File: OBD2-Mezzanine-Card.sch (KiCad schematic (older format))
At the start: 18 parts, among them P1 CONN_02X20

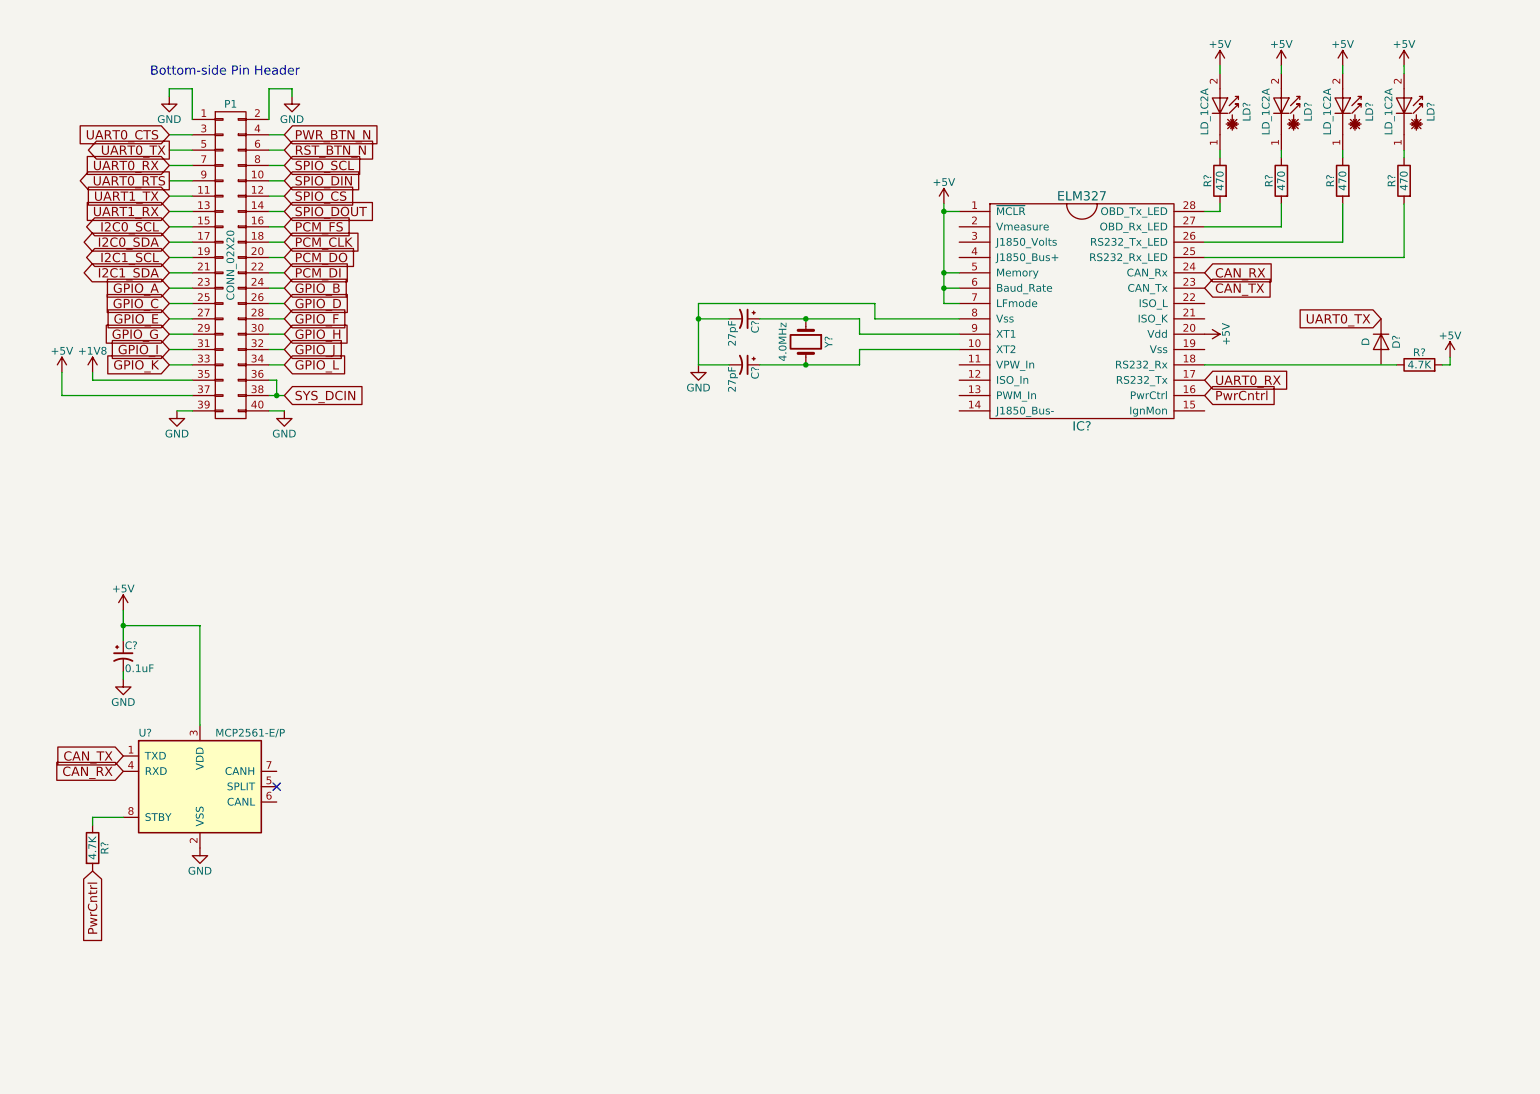
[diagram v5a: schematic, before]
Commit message: sch: Add some more connections
Signed-off-by: Alistair Francis <alistair@alistair23.me>
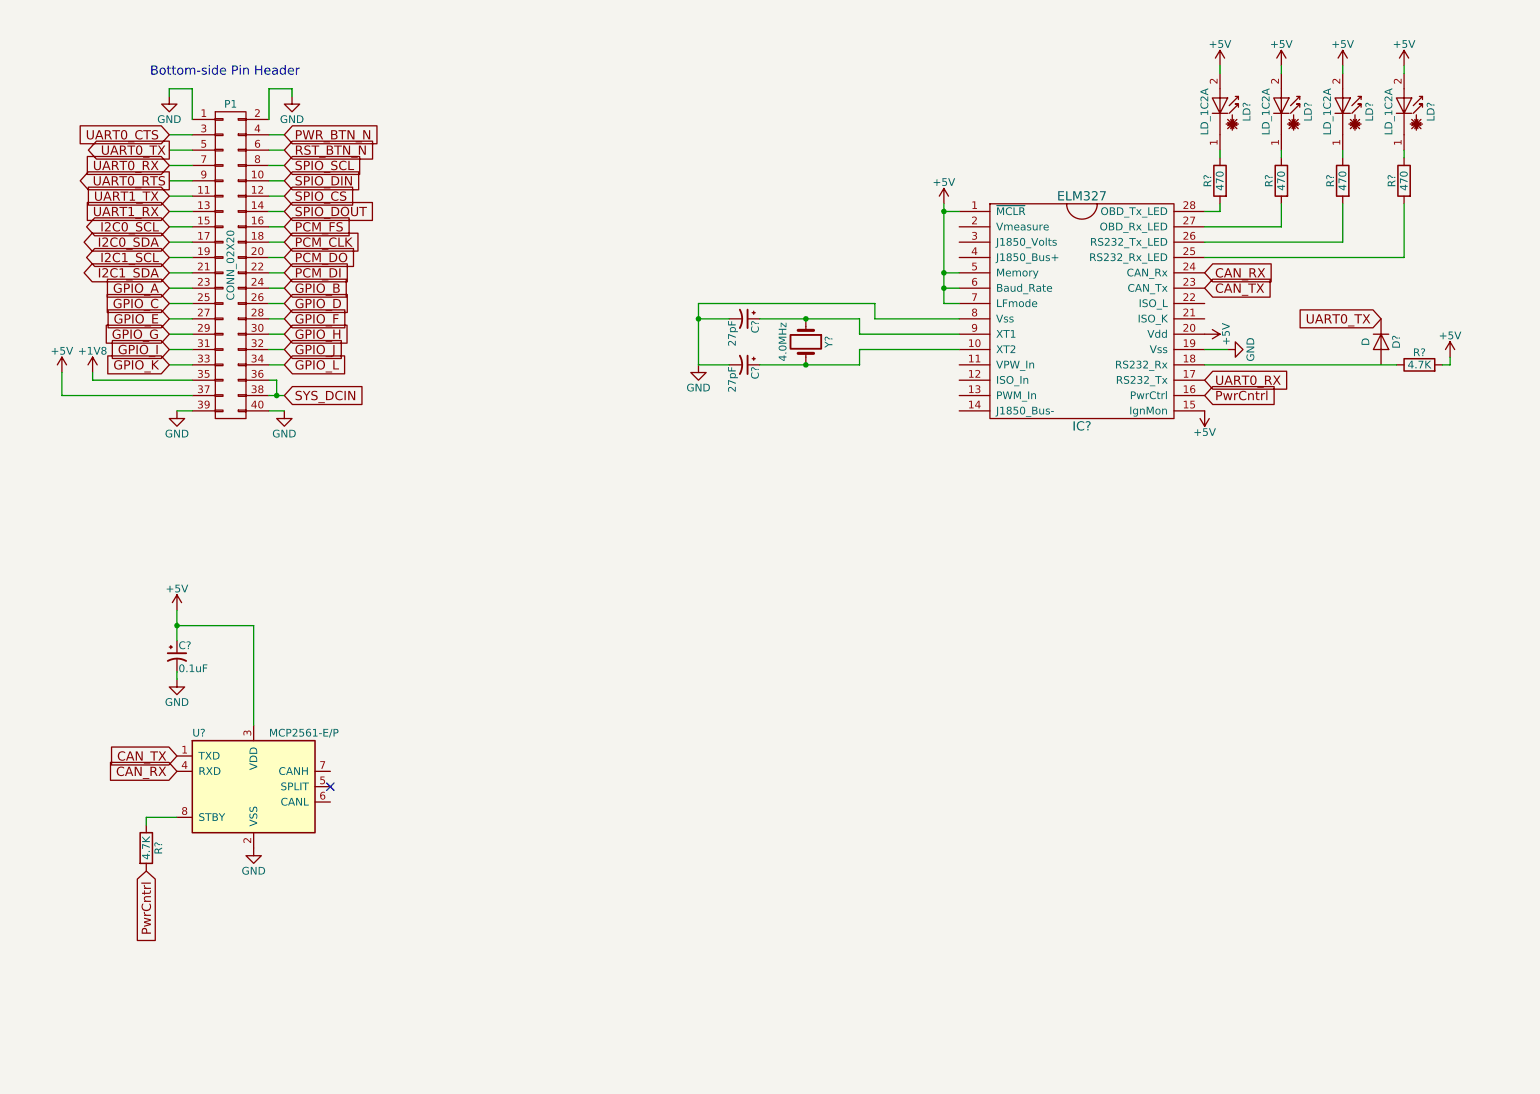
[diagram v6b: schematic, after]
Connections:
- net +5V: now also IC?.15 (IgnMon)
- net GND: now also IC?.19 (Vss)
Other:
- moved on the sheet: C?, R?, U?
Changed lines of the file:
@@
 L MCP2561-E/P U?
 U 1 1 5AA61DC4
-P 1900 5700
-F 0 "U?" H 1500 6050 50  0000 L CNN
-F 1 "MCP2561-E/P" H 2000 6050 50  0000 L CNN
-F 2 "Housings_DIP:DIP-8_W7.62mm" H 1900 5200 50  0001 C CIN
-F 3 "" H 1900 5700 50  0001 C CNN
-	1    1900 5700
+P 2250 5700
+F 0 "U?" H 1850 6050 50  0000 L CNN
+F 1 "MCP2561-E/P" H 2350 6050 50  0000 L CNN
+F 2 "Housings_DIP:DIP-8_W7.62mm" H 2250 5200 50  0001 C CIN
+F 3 "" H 2250 5700 50  0001 C CNN
+	1    2250 5700
 	1    0    0    -1
 $EndComp
-Text GLabel 1400 5600 0    60   Input ~ 0
+Text GLabel 1750 5600 0    60   Input ~ 0
 CAN_RX
 Text GLabel 8450 2350 2    60   Input ~ 0
@@
 Text GLabel 8450 2450 2    60   Input ~ 0
 CAN_TX
-Text GLabel 1400 5500 0    60   Input ~ 0
+Text GLabel 1750 5500 0    60   Input ~ 0
 CAN_TX
 $Comp
 L GND #PWR?
 U 1 1 5AA5FF31
-P 1900 6100
-F 0 "#PWR?" H 1900 5850 50  0001 C CNN
-F 1 "GND" H 1900 5950 50  0000 C CNN
-F 2 "" H 1900 6100 50  0001 C CNN
-F 3 "" H 1900 6100 50  0001 C CNN
-	1    1900 6100
+P 2250 6100
+F 0 "#PWR?" H 2250 5850 50  0001 C CNN
+F 1 "GND" H 2250 5950 50  0000 C CNN
+F 2 "" H 2250 6100 50  0001 C CNN
+F 3 "" H 2250 6100 50  0001 C CNN
+	1    2250 6100
 	1    0    0    -1
 $EndComp
@@
 L +5V #PWR?
 U 1 1 5AA5FFA4
-P 1400 4550
-F 0 "#PWR?" H 1400 4400 50  0001 C CNN
-F 1 "+5V" H 1400 4690 50  0000 C CNN
-F 2 "" H 1400 4550 50  0001 C CNN
-F 3 "" H 1400 4550 50  0001 C CNN
-	1    1400 4550
+P 1750 4550
+F 0 "#PWR?" H 1750 4400 50  0001 C CNN
+F 1 "+5V" H 1750 4690 50  0000 C CNN
+F 2 "" H 1750 4550 50  0001 C CNN
+F 3 "" H 1750 4550 50  0001 C CNN
+	1    1750 4550
 	1    0    0    -1
 $EndComp
@@
 L CP1_Small C?
 U 1 1 5AA5FFD8
-P 1400 4850
-F 0 "C?" H 1410 4920 50  0000 L CNN
-F 1 "0.1uF" H 1410 4770 50  0000 L CNN
-F 2 "" H 1400 4850 50  0001 C CNN
-F 3 "" H 1400 4850 50  0001 C CNN
-	1    1400 4850
+P 1750 4850
+F 0 "C?" H 1760 4920 50  0000 L CNN
+F 1 "0.1uF" H 1760 4770 50  0000 L CNN
+F 2 "" H 1750 4850 50  0001 C CNN
+F 3 "" H 1750 4850 50  0001 C CNN
+	1    1750 4850
 	1    0    0    -1
 $EndComp
@@
 L GND #PWR?
 U 1 1 5AA600BE
-P 1400 5000
-F 0 "#PWR?" H 1400 4750 50  0001 C CNN
-F 1 "GND" H 1400 4850 50  0000 C CNN
-F 2 "" H 1400 5000 50  0001 C CNN
-F 3 "" H 1400 5000 50  0001 C CNN
-	1    1400 5000
+P 1750 5000
+F 0 "#PWR?" H 1750 4750 50  0001 C CNN
+F 1 "GND" H 1750 4850 50  0000 C CNN
+F 2 "" H 1750 5000 50  0001 C CNN
+F 3 "" H 1750 5000 50  0001 C CNN
+	1    1750 5000
 	1    0    0    -1
 $EndComp
 Wire Wire Line
-	1400 4550 1400 4750
+	1750 4550 1750 4750
 Wire Wire Line
-	1400 4950 1400 5000
+	1750 4950 1750 5000
 Wire Wire Line
-	1400 4650 1900 4650
+	1750 4650 2250 4650
 Wire Wire Line
-	1900 4650 1900 5300
-Connection ~ 1400 4650
+	2250 4650 2250 5300
+Connection ~ 1750 4650
 $Comp
 L R R?
 U 1 1 5AA6032D
-P 1200 6100
-F 0 "R?" V 1280 6100 50  0000 C CNN
-F 1 "4.7K" V 1200 6100 50  0000 C CNN
-F 2 "" V 1130 6100 50  0001 C CNN
-F 3 "" H 1200 6100 50  0001 C CNN
-	1    1200 6100
+P 1550 6100
+F 0 "R?" V 1630 6100 50  0000 C CNN
+F 1 "4.7K" V 1550 6100 50  0000 C CNN
+F 2 "" V 1480 6100 50  0001 C CNN
+F 3 "" H 1550 6100 50  0001 C CNN
+	1    1550 6100
 	1    0    0    -1
 $EndComp
 Text GLabel 8450 3150 2    60   Input ~ 0
 PwrCntrl
-Text GLabel 1200 6250 3    60   Input ~ 0
+Text GLabel 1550 6250 3    60   Input ~ 0
 PwrCntrl
 Wire Wire Line
-	1400 5900 1200 5900
+	1750 5900 1550 5900
 Wire Wire Line
-	1200 5900 1200 5950
-NoConn ~ 2400 5700
+	1550 5900 1550 5950
+NoConn ~ 2750 5700
+$Comp
+L +5V #PWR?
+U 1 1 5AA61411
+P 8450 3250
+F 0 "#PWR?" H 8450 3100 50  0001 C CNN
+F 1 "+5V" H 8450 3390 50  0000 C CNN
+F 2 "" H 8450 3250 50  0001 C CNN
+F 3 "" H 8450 3250 50  0001 C CNN
+	1    8450 3250
+	-1   0    0    1
+$EndComp
+$Comp
+L GND #PWR?
+U 1 1 5AA61537
+P 8600 2850
+F 0 "#PWR?" H 8600 2600 50  0001 C CNN
+F 1 "GND" H 8600 2700 50  0000 C CNN
+F 2 "" H 8600 2850 50  0001 C CNN
+F 3 "" H 8600 2850 50  0001 C CNN
+	1    8600 2850
+	0    -1   -1   0
+$EndComp
+Wire Wire Line
+	8600 2850 8450 2850
 $EndSCHEMATC

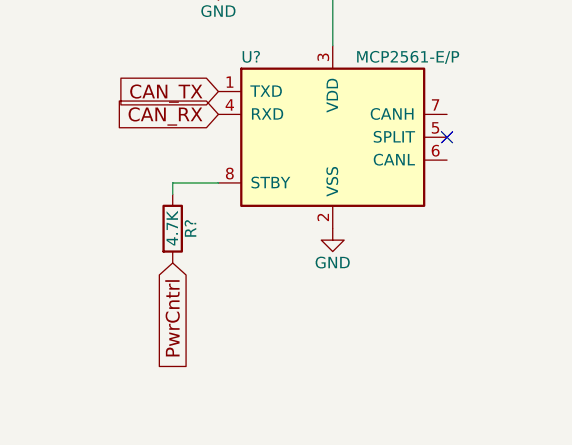
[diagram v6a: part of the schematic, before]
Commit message: sch: Fixup a mistake
Signed-off-by: Alistair Francis <alistair@alistair23.me>
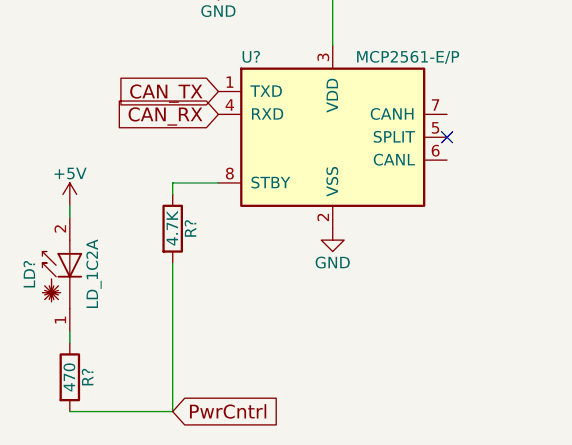
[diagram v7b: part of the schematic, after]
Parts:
- added LD?: LD_1C2A, symbol Laserdiode_1C2A
- added R?: 470, symbol R
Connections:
- net +5V: now also LD?.2 (A)
- net PwrCntrl: now also R?.2
- new net: LD?.1 (K), R?.1
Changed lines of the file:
@@
 Text GLabel 8450 3150 2    60   Input ~ 0
 PwrCntrl
-Text GLabel 1550 6250 3    60   Input ~ 0
+Text GLabel 1550 6900 2    60   Input ~ 0
 PwrCntrl
 Wire Wire Line
@@
 Wire Wire Line
 	8600 2850 8450 2850
+$Comp
+L +5V #PWR?
+U 1 1 5AA61B64
+P 1100 6000
+F 0 "#PWR?" H 1100 5850 50  0001 C CNN
+F 1 "+5V" H 1100 6140 50  0000 C CNN
+F 2 "" H 1100 6000 50  0001 C CNN
+F 3 "" H 1100 6000 50  0001 C CNN
+	1    1100 6000
+	1    0    0    -1
+$EndComp
+$Comp
+L Laserdiode_1C2A LD?
+U 1 1 5AA61B9C
+P 1100 6250
+F 0 "LD?" H 1050 6425 50  0000 C CNN
+F 1 "LD_1C2A" H 1050 6150 50  0000 C CNN
+F 2 "" H 1000 6225 50  0001 C CNN
+F 3 "" H 1130 6050 50  0001 C CNN
+	1    1100 6250
+	0    -1   -1   0
+$EndComp
+$Comp
+L R R?
+U 1 1 5AA63138
+P 1100 6750
+F 0 "R?" V 1180 6750 50  0000 C CNN
+F 1 "470" V 1100 6750 50  0000 C CNN
+F 2 "" V 1030 6750 50  0001 C CNN
+F 3 "" H 1100 6750 50  0001 C CNN
+	1    1100 6750
+	1    0    0    -1
+$EndComp
+Wire Wire Line
+	1100 6000 1100 6050
+Wire Wire Line
+	1100 6550 1100 6600
+Wire Wire Line
+	1100 6900 1550 6900
+Wire Wire Line
+	1550 6900 1550 6250
 $EndSCHEMATC

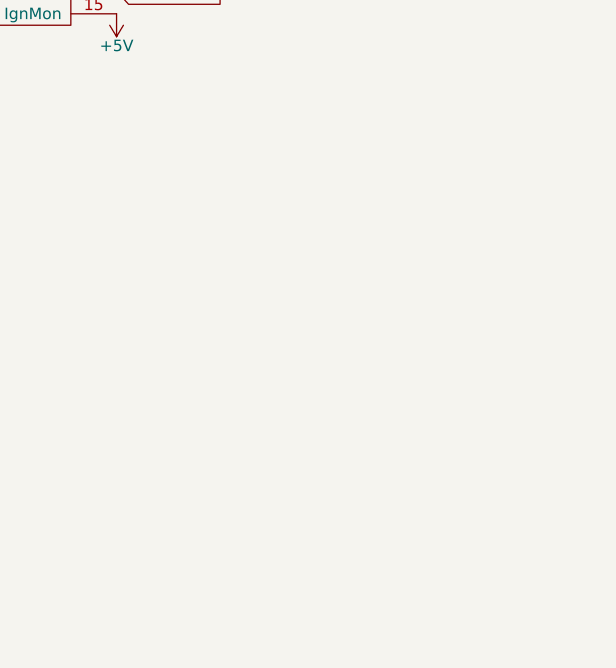
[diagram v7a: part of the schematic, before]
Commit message: sch: Add the OBD2 breakout
Signed-off-by: Alistair Francis <alistair@alistair23.me>
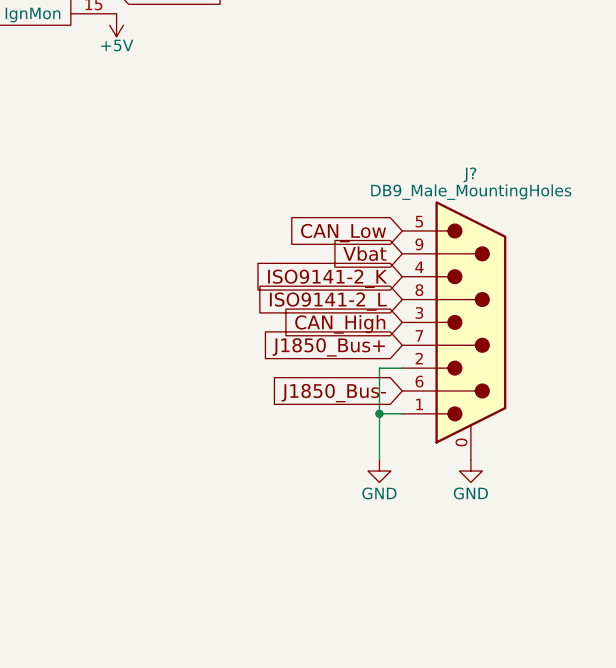
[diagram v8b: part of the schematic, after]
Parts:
- added J?: DB9_Male_MountingHoles, symbol DB9_Male_MountingHoles
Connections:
- net GND: now also J?.0 (PAD), J?.1, J?.2
- new net CAN_High: J?.3
- new net CAN_Low: J?.5
- new net ISO9141-2_K: J?.4
- new net ISO9141-2_L: J?.8
- new net J1850_Bus+: J?.7
- new net J1850_Bus-: J?.6
- new net Vbat: J?.9
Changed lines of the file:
@@
 Wire Wire Line
 	1550 6900 1550 6250
+$Comp
+L DB9_Male_MountingHoles J?
+U 1 1 5AA9B3F8
+P 10000 4600
+F 0 "J?" H 10000 5250 50  0000 C CNN
+F 1 "DB9_Male_MountingHoles" H 10000 5175 50  0000 C CNN
+F 2 "" H 10000 4600 50  0001 C CNN
+F 3 "" H 10000 4600 50  0001 C CNN
+	1    10000 4600
+	1    0    0    -1
+$EndComp
+$Comp
+L GND #PWR?
+U 1 1 5AA9B455
+P 10000 5200
+F 0 "#PWR?" H 10000 4950 50  0001 C CNN
+F 1 "GND" H 10000 5050 50  0000 C CNN
+F 2 "" H 10000 5200 50  0001 C CNN
+F 3 "" H 10000 5200 50  0001 C CNN
+	1    10000 5200
+	1    0    0    -1
+$EndComp
+Text GLabel 9700 4300 0    60   Input ~ 0
+Vbat
+Text GLabel 9700 4500 0    60   Input ~ 0
+ISO9141-2_L
+Text GLabel 9700 4200 0    60   Input ~ 0
+CAN_Low
+Text GLabel 9700 4900 0    60   Input ~ 0
+J1850_Bus-
+Text GLabel 9700 4400 0    60   Input ~ 0
+ISO9141-2_K
+Text GLabel 9700 4600 0    60   Input ~ 0
+CAN_High
+$Comp
+L GND #PWR?
+U 1 1 5AA9C121
+P 9600 5200
+F 0 "#PWR?" H 9600 4950 50  0001 C CNN
+F 1 "GND" H 9600 5050 50  0000 C CNN
+F 2 "" H 9600 5200 50  0001 C CNN
+F 3 "" H 9600 5200 50  0001 C CNN
+	1    9600 5200
+	1    0    0    -1
+$EndComp
+Wire Wire Line
+	9700 4800 9600 4800
+Wire Wire Line
+	9600 4800 9600 5200
+Wire Wire Line
+	9600 5000 9700 5000
+Connection ~ 9600 5000
+Text GLabel 9700 4700 0    60   Input ~ 0
+J1850_Bus+
 $EndSCHEMATC
